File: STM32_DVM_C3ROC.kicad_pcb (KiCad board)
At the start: 4 copper layers, 65 x 56 mm, 170 parts, among them IC2 MCP6002, IC3 MCP6002, IC4 MCP6002, J1 40HAT, J2 USB_B_Micro, Q1 Crystal_GND23, T1 MMUN2214, T2 MMUN2214, T3 MMUN2214, T4 MMUN2214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

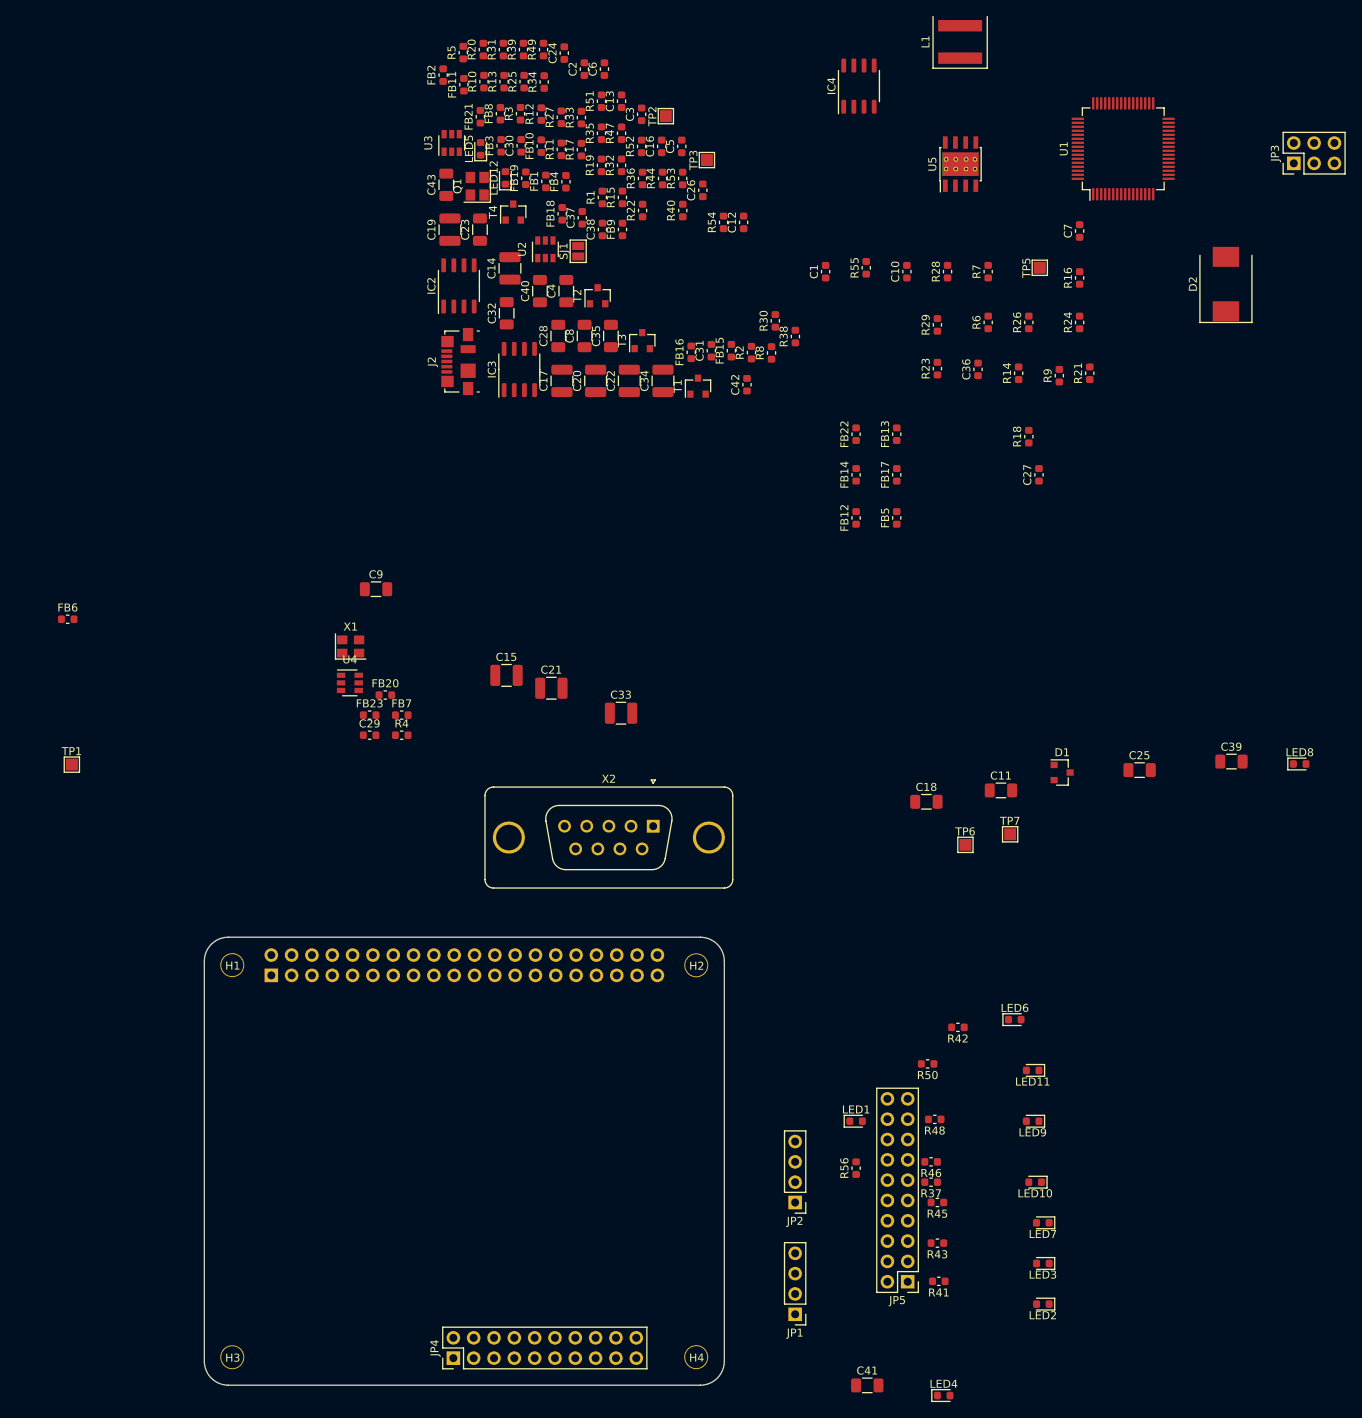
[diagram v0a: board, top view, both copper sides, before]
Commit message: Platzierung 90 % komplett
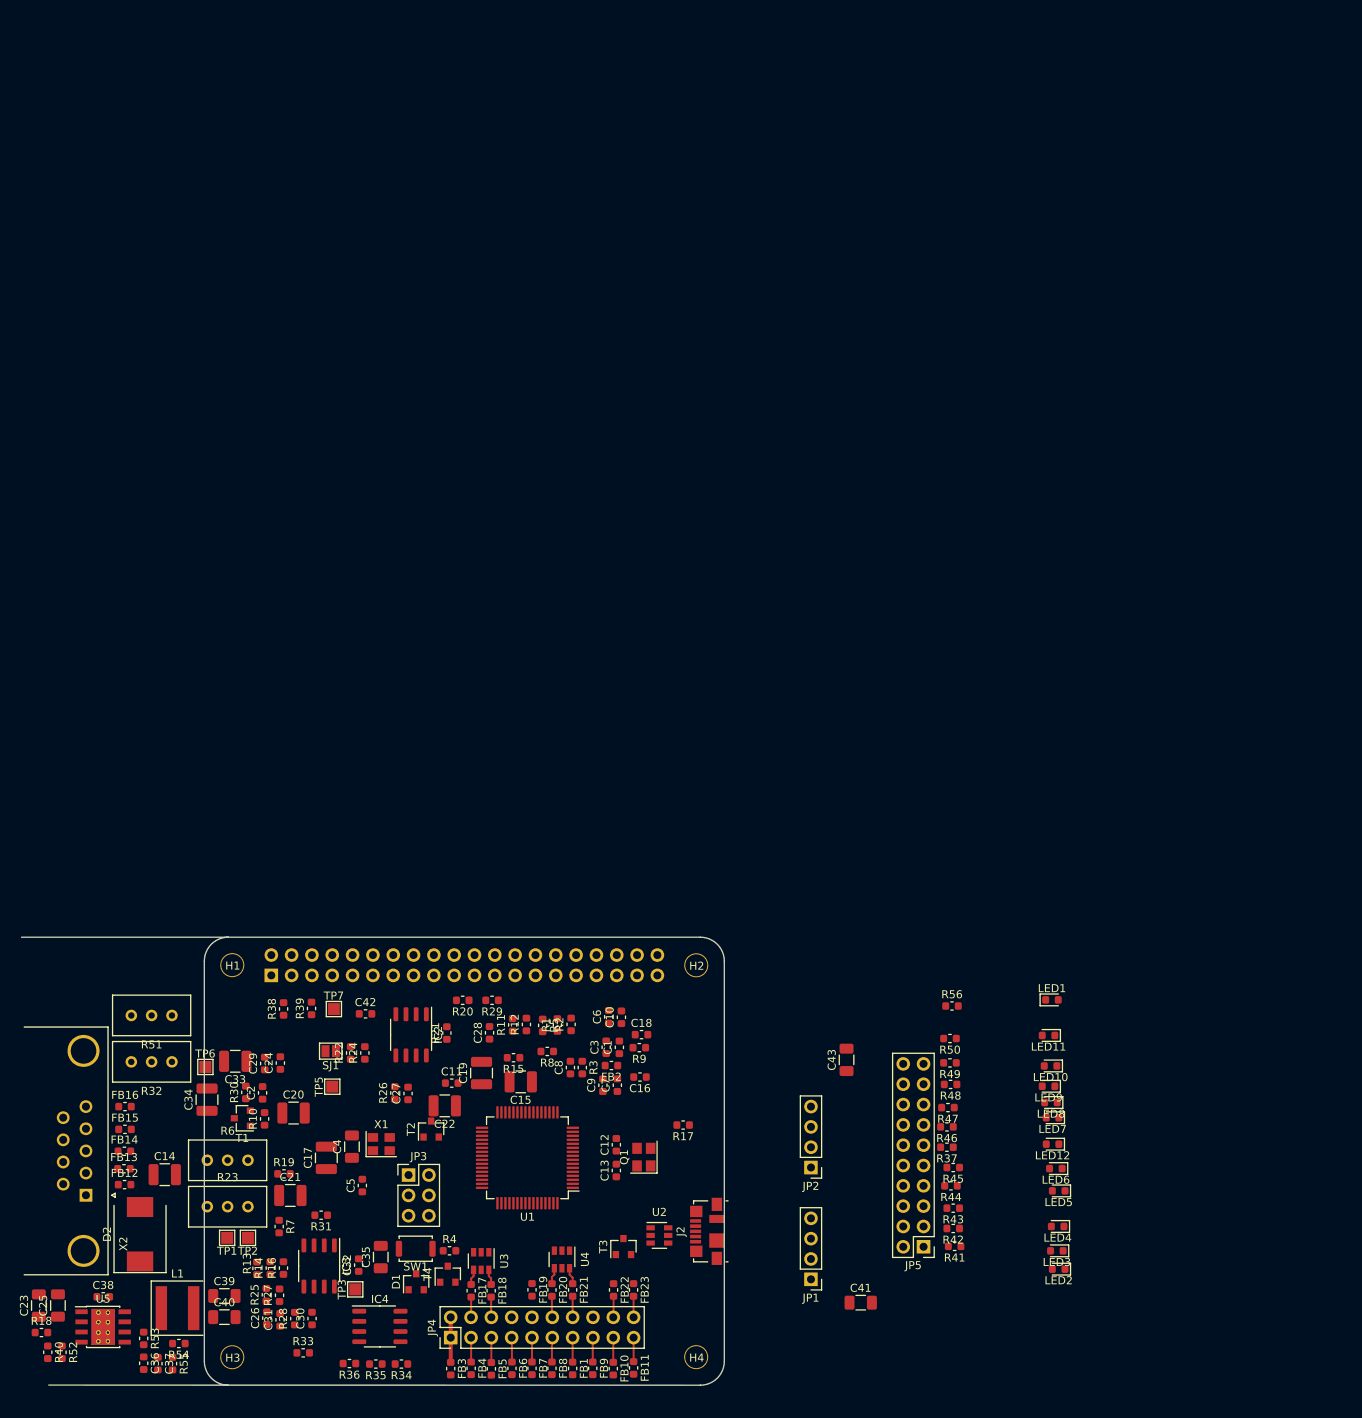
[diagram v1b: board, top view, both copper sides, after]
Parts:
- added SW1: SW_Push, Button_Switch_SMD:SW_Push_SPST_NO_Alps_SKRK, F.Cu at (105.0, 99.8)
- C11, C18, C28, C32, C8, C9: footprint Capacitor_SMD:C_1206_3216Metric -> Capacitor_SMD:C_0603_1608Metric
- R23, R32, R51, R6: footprint Resistor_SMD:R_0603_1608Metric -> Potentiometer_THT:Potentiometer_Bourns_3296W_Vertical
- X2: footprint Connector_Dsub:DSUB-9_Female_Vertical_P2.77x2.84mm_MountingHoles -> Connector_Dsub:DSUB-9_Female_Horizontal_P2.77x2.84mm_EdgePinOffset4.94mm_Housed_MountingHolesOffset7.48mm
- moved L1 186.1 mm to (75.2, 107.2), turned to 0 degrees
- moved U5 180.6 mm to (65.9, 109.5), turned to 0 degrees
- moved D2 180.4 mm to (70.5, 97.9)
- moved JP3 168.0 mm to (104.1, 90.6), turned to 0 degrees
- moved R52 167.2 mm to (60.8, 112.7), turned to 270 degrees
- moved R18 166.7 mm to (58.2, 110.2), turned to 0 degrees
- moved IC4 166.2 mm to (100.5, 109.5), turned to 0 degrees
- moved R40 163.3 mm to (59.0, 112.7), turned to 270 degrees
- moved C36 162.2 mm to (71.0, 114.1), turned to 270 degrees
- moved R55 162.1 mm to (74.6, 114.1), turned to 270 degrees
- moved FB11 161.8 mm to (132.2, 114.7), turned to 270 degrees
- moved R34 161.2 mm to (103.2, 114.2), turned to 180 degrees
- moved R53 159.9 mm to (71.0, 111.0), turned to 270 degrees
- moved R16 158.8 mm to (88.4, 102.2)
- moved R33 158.3 mm to (90.9, 112.8), turned to 0 degrees
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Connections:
- C1 pad 2: INHIBIT -> GND
- C10 pad 2: INHIBIT -> GND
- C11 pad 2: INHIBIT -> GND
- C12 pad 2: INHIBIT -> GND
- C13 pad 2: INHIBIT -> GND
- C15 pad 2: INHIBIT -> GND
- C16 pad 2: INHIBIT -> GND
- C17 pad 2: INHIBIT -> GND
- C18 pad 2: INHIBIT -> GND
- C19 pad 1: Net-(C19-Pad1) -> TXA
- C2 pad 2: INHIBIT -> GND
- C21 pad 2: INHIBIT -> GND
- C22 pad 2: INHIBIT -> GND
- C23 pad 2: INHIBIT -> GND
- C24 pad 2: INHIBIT -> GND
- C25 pad 2: INHIBIT -> GND
- C26 pad 2: INHIBIT -> GND
- C28 pad 2: INHIBIT -> GND
- C29 pad 2: INHIBIT -> GND
- C3 pad 2: INHIBIT -> GND
- C31 pad 2: INHIBIT -> GND
- C32 pad 2: INHIBIT -> GND
- C35 pad 2: INHIBIT -> GND
- C36 pad 2: INHIBIT -> GND
- C37 pad 2: INHIBIT -> GND
- C39 pad 2: INHIBIT -> GND
- C4 pad 2: INHIBIT -> GND
- C40 pad 2: INHIBIT -> GND
- C42 pad 2: INHIBIT -> GND
- C6 pad 2: INHIBIT -> GND
- C7 pad 2: INHIBIT -> GND
- C8 pad 2: INHIBIT -> GND
- C9 pad 2: INHIBIT -> GND
- D2 pad 2: INHIBIT -> GND
- IC2 pad 4: INHIBIT -> GND
- IC3 pad 4: INHIBIT -> GND
- IC4 pad 4: INHIBIT -> GND
- J1 pad 14: INHIBIT -> GND
- J1 pad 20: INHIBIT -> GND
- J1 pad 25: INHIBIT -> GND
- J1 pad 30: INHIBIT -> GND
- J1 pad 34: INHIBIT -> GND
- J1 pad 39: INHIBIT -> GND
- J1 pad 6: INHIBIT -> GND
- J1 pad 9: INHIBIT -> GND
- J2 pad 5: INHIBIT -> GND
- J2 pad 6: INHIBIT -> GND
- JP3 pad 3: INHIBIT -> GND
- JP3 pad 5: INHIBIT -> GND
- JP4 pad 16: INHIBIT -> GND
- JP4 pad 8: INHIBIT -> GND
- Q1 pad 2: INHIBIT -> GND
- Q1 pad 3: INHIBIT -> GND
- Q1 pad 4: Net-(Q1-Pad4) -> Net-(C13-Pad1)
- R12 pad 2: INHIBIT -> GND
- R14 pad 2: INHIBIT -> GND
- R30 pad 1: Net-(R30-Pad1) -> INHIBIT
- R30 pad 2: INHIBIT -> GND
- R32 pad 1: INHIBIT -> GND
- R36 pad 2: INHIBIT -> GND
- R40 pad 2: INHIBIT -> GND
- R5 pad 2: INHIBIT -> GND
- R51 pad 1: INHIBIT -> GND
- R52 pad 2: INHIBIT -> GND
- R55 pad 2: INHIBIT -> GND
- R7 pad 2: INHIBIT -> GND
- R8 pad 2: INHIBIT -> GND
- T1 pad 2: Net-(R30-Pad1) -> INHIBIT
- T2 pad 2: INHIBIT -> GND
- T3 pad 2: INHIBIT -> GND
- U1 pad 12: INHIBIT -> GND
- U1 pad 18: INHIBIT -> GND
- U1 pad 31: INHIBIT -> GND
- U1 pad 47: INHIBIT -> GND
- U1 pad 63: INHIBIT -> GND
- U2 pad 2: INHIBIT -> GND
- U3 pad 2: INHIBIT -> GND
- U4 pad 2: INHIBIT -> GND
- U5 pad 7: INHIBIT -> GND
- U5 pad 9: INHIBIT -> GND
- X1 pad 2: INHIBIT -> GND
- X2 pad 0: INHIBIT -> GND
- X2 pad 8: INHIBIT -> GND
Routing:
- net Net-(FB3-Pad1): track 0.00 -> 5.63 mm
- net Net-(FB5-Pad1): track 0.00 -> 3.11 mm
- net Net-(FB10-Pad1): track 0.00 -> 3.09 mm
- net Net-(FB8-Pad1): track 0.00 -> 3.07 mm
- net Net-(FB6-Pad1): track 0.00 -> 3.07 mm
- net Net-(FB1-Pad1): track 0.00 -> 3.06 mm
- net Net-(FB9-Pad1): track 0.00 -> 3.06 mm
- net Net-(FB4-Pad1): track 0.00 -> 3.06 mm
- net Net-(FB7-Pad1): track 0.00 -> 3.05 mm
- net Net-(FB11-Pad1): track 0.00 -> 3.00 mm
- net Net-(FB20-Pad2): track 0.00 -> 2.65 mm
- net Net-(FB22-Pad2): track 0.00 -> 2.64 mm
- net Net-(FB23-Pad2): track 0.00 -> 2.63 mm
- net Net-(FB21-Pad2): track 0.00 -> 2.63 mm
- net Net-(FB18-Pad2): track 0.00 -> 2.54 mm
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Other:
- board size 65 x 56 mm -> 87.8 x 56 mm

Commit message: LCSC Part List angelegt, Footprints angepasst
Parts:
- removed R17: 10K, Resistor_SMD:R_0603_1608Metric
- C11, C18, C28, C32, C8, C9: footprint Capacitor_SMD:C_0603_1608Metric -> Capacitor_SMD:C_1206_3216Metric
- C39, C40: footprint Capacitor_SMD:C_1206_3216Metric -> Capacitor_SMD:C_1210_3225Metric
- L1: footprint Inductor_SMD:L_Coilcraft_XAL60xx_6.36x6.56mm -> Inductor_SMD:L_Bourns_SRP7028A_7.3x6.6mm
- Q1: value Crystal_GND23 -> Crystal_GND24
- X1: value ASE-12MHz -> IQXO-70; footprint Oscillator:Oscillator_SMD_Abracon_ASE-4Pin_3.2x2.5mm -> Oscillator:Oscillator_SMD_IQD_IQXO70-4Pin_7.5x5.0mm
- moved C5 7.92 mm to (101.2, 84.5)
- moved C4 5.51 mm to (97.5, 81.5)
- moved X1 4.96 mm to (97.4, 90.4)
- moved C17 4.49 mm to (89.3, 87.9)
- moved Q1 0.54 mm to (134.0, 88.4), turned to 0 degrees
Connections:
- Q1 pad 3: GND -> Net-(C13-Pad1)
- Q1 pad 4: Net-(C13-Pad1) -> GND

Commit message: Layout 80 %, kleine Korrekturen
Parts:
- R10, R3, R4: value 10K -> 10k
- R18: value 10k -> 523k
- R40: value 10k -> 82k
- SW1: footprint Button_Switch_SMD:SW_Push_SPST_NO_Alps_SKRK -> Button_Switch_SMD:SW_SPST_SKQG_WithoutStem
- TP1, TP2, TP3, TP5, TP6, TP7: footprint TestPoint:TestPoint_Pad_1.5x1.5mm -> TestPoint:TestPoint_Pad_D1.5mm
- moved R29 39.7 mm to (98.7, 105.1)
- moved C28 35.9 mm to (96.0, 103.7)
- moved R9 30.5 mm to (102.8, 79.5), turned to 90 degrees
- moved C18 29.5 mm to (103.8, 74.9), turned to 90 degrees
- moved C6 27.4 mm to (126.4, 98.1), turned to 180 degrees
- moved R5 25.6 mm to (108.4, 94.2), turned to 0 degrees
- moved R31 23.5 mm to (106.8, 114.8), turned to 90 degrees
- moved C29 13.3 mm to (99.1, 79.5), turned to 270 degrees
- moved C2 12.4 mm to (97.3, 84.9)
- moved R7 11.4 mm to (88.6, 85.6), turned to 0 degrees
- moved C22 11.1 mm to (113.0, 71.8), turned to 0 degrees
- moved C7 10.3 mm to (137.0, 71.6), turned to 180 degrees
- moved C5 10.1 mm to (104.2, 94.1), turned to 0 degrees
- moved R12 9.88 mm to (109.0, 72.5), turned to 180 degrees
- moved C32 9.30 mm to (103.1, 109.5), turned to 270 degrees
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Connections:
- FB14 pad 2: INIHIBIT_R -> INHIBIT_R
- T2 pad 1: PTT_R -> PTT
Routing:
- net GND: track 0.00 -> 421.7 mm, vias 0 -> 37
- net +3V3: track 0.00 -> 167.4 mm, vias 0 -> 11
- net +5V: track 0.00 -> 110.4 mm, vias 0 -> 4
- net PTT: track 0.00 -> 42.0 mm, vias 0 -> 2
- net LED_FM: track 0.00 -> 39.6 mm, vias 0 -> 2
- net RSSI: track 0.00 -> 39.0 mm, vias 0 -> 1
- net LED_P25: track 0.00 -> 38.7 mm, vias 0 -> 2
- net LED_COS: track 0.00 -> 38.1 mm, vias 0 -> 2
- net LED_HB: track 0.00 -> 36.7 mm, vias 0 -> 2
- net +BATT: track 0.00 -> 35.8 mm, vias 0 -> 2
- net LED_DMR: track 0.00 -> 34.6 mm, vias 0 -> 2
- net LED_YSF: track 0.00 -> 34.6 mm, vias 0 -> 2
- net LED_DSTAR: track 0.00 -> 34.2 mm, vias 0 -> 2
- net Net-(IC3-Pad1): track 0.00 -> 33.4 mm, vias 0 -> 3
- net SDA: track 0.00 -> 29.5 mm
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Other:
- board size 87.8 x 56 mm -> 85.2 x 56 mm

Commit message: Layout fertig für review
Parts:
- added H5: 3mm, project_footprints:NPTH_3mm_ID, F.Cu at (148.0, 64.5)
- added H6: 3mm, project_footprints:NPTH_3mm_ID, F.Cu at (148.0, 113.1)
- added H7: 3mm, project_footprints:NPTH_3mm_ID, F.Cu at (165.0, 64.5)
- added H8: 3mm, project_footprints:NPTH_3mm_ID, F.Cu at (165.0, 113.1)
- JP1, JP2, JP5: moved to B.Cu
- moved LED1 44.5 mm to (165.0, 108.6)
- moved LED11 37.2 mm to (165.0, 105.0)
- moved LED3 37.0 mm to (165.0, 69.0)
- moved R50 34.9 mm to (158.6, 105.9)
- moved LED4 31.7 mm to (165.0, 72.6)
- moved C41 29.8 mm to (149.4, 78.9), turned to 270 degrees
- moved LED10 28.5 mm to (165.0, 97.8)
- moved R49 27.2 mm to (158.6, 100.4)
- moved JP1 26.4 mm to (146.4, 78.5)
- moved LED5 26.1 mm to (165.0, 76.2)
- moved JP5 25.8 mm to (155.0, 77.5)
- moved C3 25.3 mm to (112.8, 94.2), turned to 180 degrees
- moved LED9 24.1 mm to (165.0, 94.2)
- moved R48 22.9 mm to (158.6, 97.9)
- moved LED6 22.3 mm to (165.0, 79.8)
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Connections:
- J1 pad 11: Net-(J1-Pad11) -> (no net)
- J1 pad 12: Net-(J1-Pad12) -> (no net)
- J1 pad 13: Net-(J1-Pad13) -> (no net)
- J1 pad 15: Net-(J1-Pad15) -> (no net)
- J1 pad 16: Net-(J1-Pad16) -> (no net)
- J1 pad 18: Net-(J1-Pad18) -> (no net)
- J1 pad 19: Net-(J1-Pad19) -> (no net)
- J1 pad 21: Net-(J1-Pad21) -> (no net)
- J1 pad 22: Net-(J1-Pad22) -> (no net)
- J1 pad 23: Net-(J1-Pad23) -> (no net)
- J1 pad 24: Net-(J1-Pad24) -> (no net)
- J1 pad 26: Net-(J1-Pad26) -> (no net)
- J1 pad 27: Net-(J1-Pad27) -> (no net)
- J1 pad 28: Net-(J1-Pad28) -> (no net)
- J1 pad 29: Net-(J1-Pad29) -> (no net)
- J1 pad 31: Net-(J1-Pad31) -> (no net)
- J1 pad 32: Net-(J1-Pad32) -> (no net)
- J1 pad 33: Net-(J1-Pad33) -> (no net)
- J1 pad 35: Net-(J1-Pad35) -> (no net)
- J1 pad 36: Net-(J1-Pad36) -> (no net)
- J1 pad 37: Net-(J1-Pad37) -> (no net)
- J1 pad 7: Net-(J1-Pad7) -> (no net)
- J2 pad 4: Net-(J2-Pad4) -> (no net)
- U1 pad 10: Net-(U1-Pad10) -> (no net)
- U1 pad 11: Net-(U1-Pad11) -> (no net)
- U1 pad 14: Net-(U1-Pad14) -> (no net)
- U1 pad 15: Net-(U1-Pad15) -> (no net)
- U1 pad 16: Net-(U1-Pad16) -> (no net)
- U1 pad 17: Net-(U1-Pad17) -> (no net)
- U1 pad 2: Net-(U1-Pad2) -> (no net)
- U1 pad 21: Net-(U1-Pad21) -> (no net)
- U1 pad 22: Net-(U1-Pad22) -> (no net)
- U1 pad 23: Net-(U1-Pad23) -> (no net)
- U1 pad 24: Net-(U1-Pad24) -> (no net)
- U1 pad 25: Net-(U1-Pad25) -> (no net)
- U1 pad 28: BOOT1 -> (no net)
- U1 pad 29: Net-(U1-Pad29) -> (no net)
- U1 pad 3: Net-(U1-Pad3) -> (no net)
- U1 pad 36: Net-(U1-Pad36) -> (no net)
- U1 pad 37: Net-(U1-Pad37) -> (no net)
- U1 pad 38: Net-(U1-Pad38) -> (no net)
- U1 pad 39: Net-(U1-Pad39) -> (no net)
- U1 pad 4: Net-(U1-Pad4) -> (no net)
- U1 pad 40: Net-(U1-Pad40) -> (no net)
- U1 pad 41: Net-(U1-Pad41) -> (no net)
- U1 pad 51: Net-(U1-Pad51) -> (no net)
- U1 pad 52: Net-(U1-Pad52) -> (no net)
- U1 pad 8: Net-(U1-Pad8) -> (no net)
- U1 pad 9: Net-(U1-Pad9) -> (no net)
- X1 pad 1: Net-(X1-Pad1) -> (no net)
- X2 pad 1: Net-(X2-Pad1) -> (no net)
- X2 pad 7: Net-(X2-Pad7) -> (no net)
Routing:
- net GND: track 421.7 -> 599.3 mm, vias 37 -> 61
- net +3V3: track 167.4 -> 284.7 mm, vias 11 -> 18
- net GNDA: track 0.00 -> 100.5 mm, vias 0 -> 13
- net +5V: track 110.4 -> 167.2 mm, vias 4 -> 9
- net BOOT0: track 0.00 -> 55.9 mm, vias 0 -> 4
- net TXD_HOST: track 26.1 -> 80.7 mm, vias 0 -> 4
- net NRST: track 0.00 -> 54.1 mm, vias 0 -> 3
- net RXA: track 6.00 -> 53.9 mm, vias 0 -> 2
- net +3.3VA: track 0.00 -> 41.1 mm, vias 0 -> 1
- net Net-(LED1-Pad2): track 0.00 -> 37.5 mm, vias 0 -> 2
- net SCL: track 26.9 -> 61.9 mm, vias 0 -> 2
- net SDA: track 29.5 -> 62.9 mm, vias 0 -> 2
- net RXD_HOST: track 28.0 -> 52.3 mm, vias 0 -> 2
- net Net-(JP5-Pad18): track 0.00 -> 22.2 mm
- net TXA: track 0.00 -> 18.8 mm
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- added copper zone on In2.Cu, net +3.3VA
- added copper zone on In2.Cu, net +3V3
- added copper zone on In2.Cu, net +5V
- added copper zone on In2.Cu, net +BATT
- added copper zone on B.Cu, net GND
- added copper zone on F.Cu, net GND
- added copper zone on B.Cu, net GNDA
- added copper zone on F.Cu, net GNDA
- removed copper zone on In2.Cu, net INHIBIT
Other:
- board size 85.2 x 56 mm -> 110 x 56 mm
- board text added: "(DG3FDM)"
- board text added: "C3ROC Edition"
- board text added: "CLIP"
- board text added: "COS"
- board text added: "DATA"
- board text added: "DMR"
- board text added: "DSTAR"
- board text added: "FM"
- board text added: "HB"
- board text added: "N3XCC"
- board text added: "NXDN"
- board text added: "P25"
- board text added: "PTT"
- board text added: "Power"
- board text added: "RFguy"
- board text added: "RSSI"
- board text added: "RX_G"
- board text added: "RX_IN"
- board text added: "SQ6POG"
- board text added: "STM32 DVM"
- board text added: "TX"
- board text added: "V4"
- board text added: "YSF"
